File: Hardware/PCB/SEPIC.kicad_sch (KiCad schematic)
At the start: 32 parts, among them Q1 AO3401A, Q2 IRFR024PBF, U1 LM3478MA

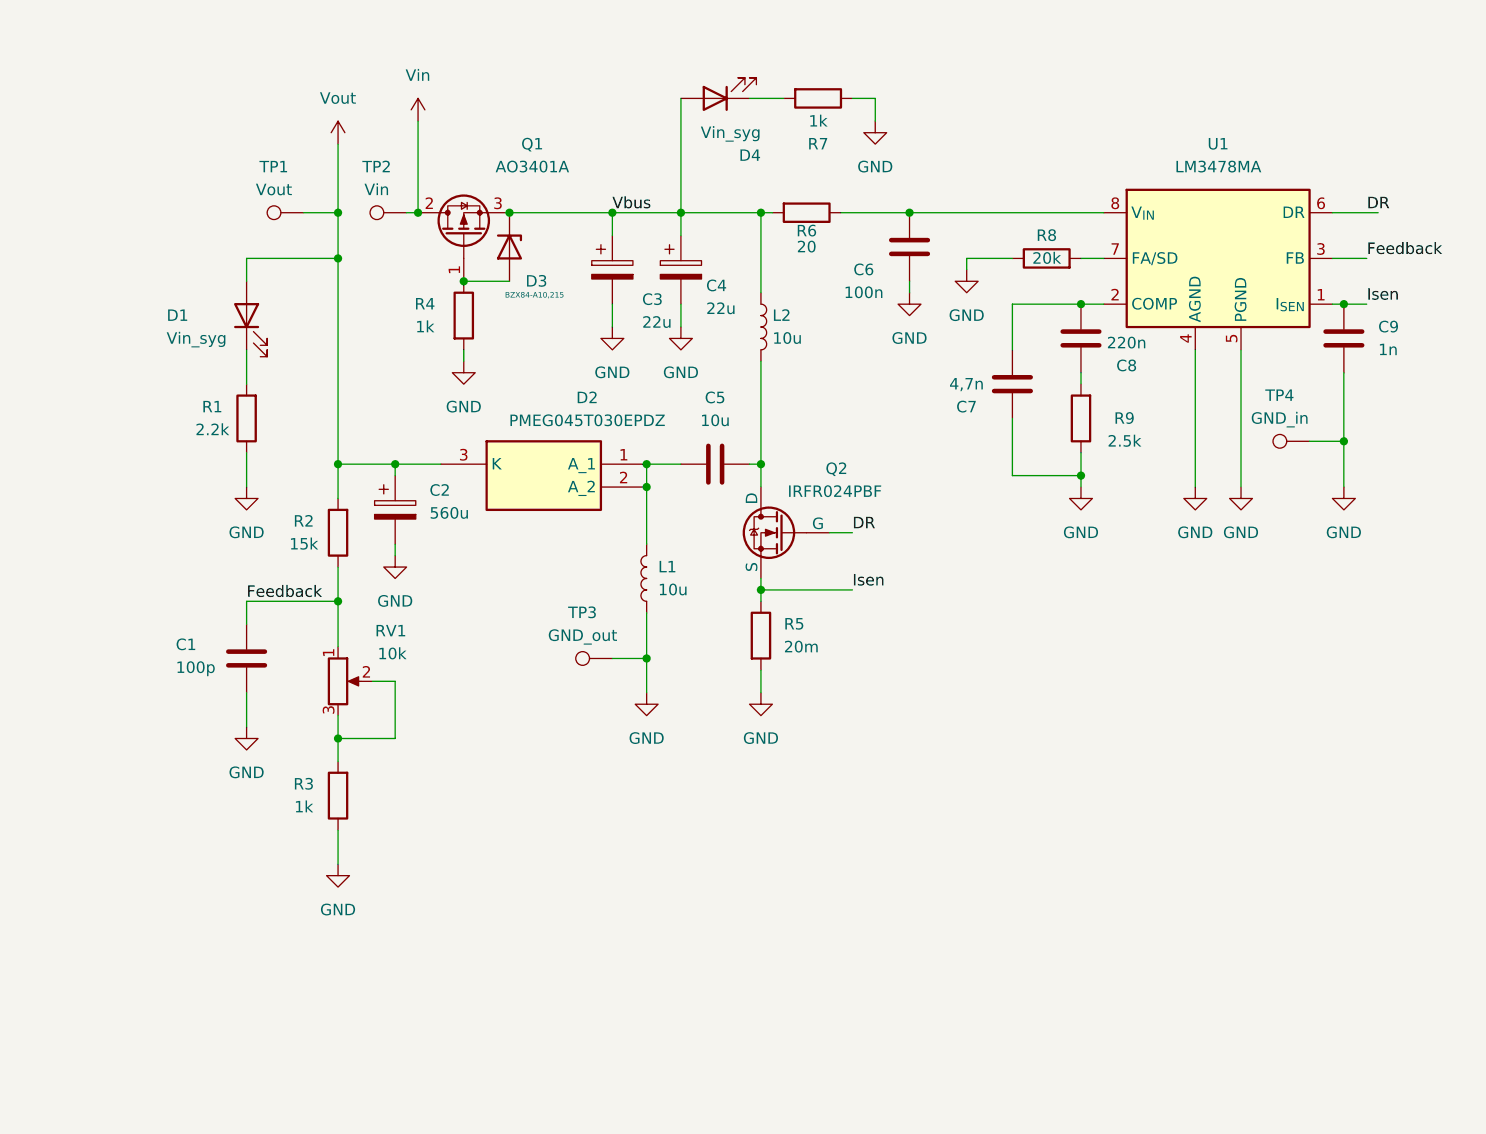
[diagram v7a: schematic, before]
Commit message: EOD PCB commit
End Of Development update, after compiling the data in a spreadsheet, I replaced the diode and the MOSFET, and also copied the calculated values for the passive components.
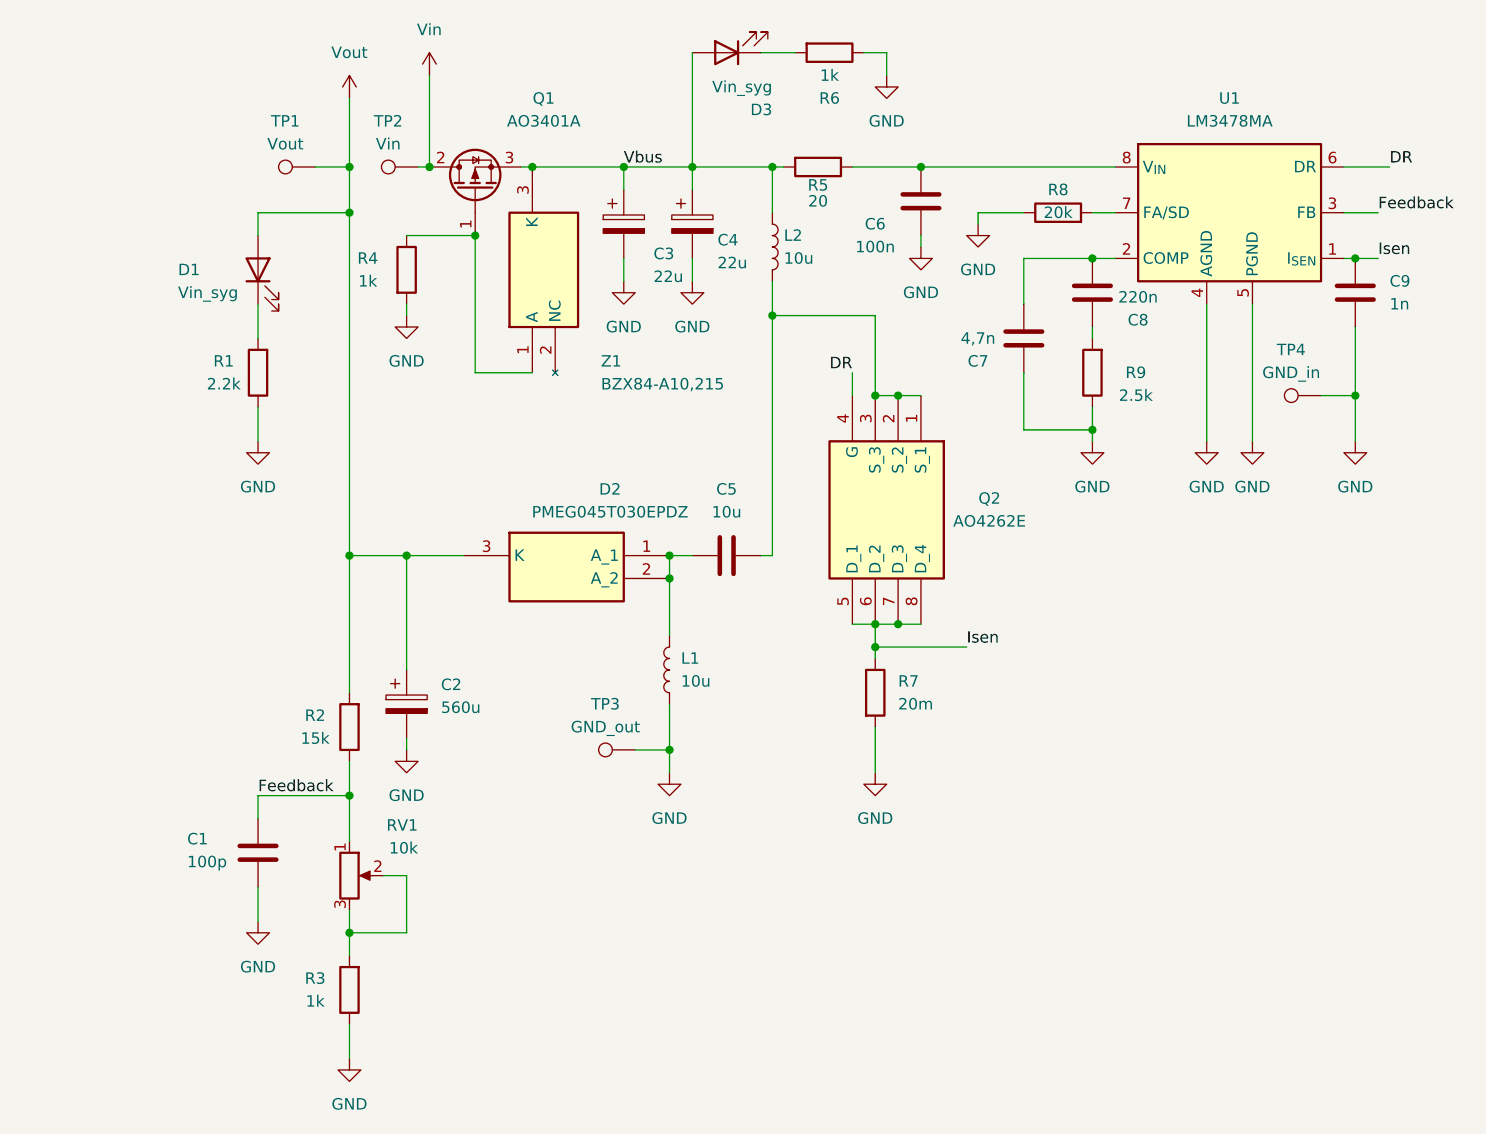
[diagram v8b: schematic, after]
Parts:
- removed D3: BZX84-A10,215, BZX84:SOT-23, symbol Device:D_Zener
- removed Q2: IRFR024PBF, IRFR024:IRFR024PBF, symbol Simulation_SPICE:NMOS
- added Q2: AO4262E, Package_SO:SOIC-8_3.9x4.9mm_P1.27mm, symbol AO4262E:AO4262E
- added Z1: BZX84-A10,215, Package_TO_SOT_SMD:SOT-23, symbol BZX84-A10_215:BZX84-A10,215
- renumbered D4 to D3, R6 to R5, R7 to R6, R5 to R7
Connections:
- net DR: now also Q2.4 (G)
- net Isen: now also Q2.5 (D_1), Q2.6 (D_2), Q2.7 (D_3), Q2.8 (D_4)
- net Vbus: now also Z1.3 (K)
- net at C5.2, L2.2: now also Q2.1 (S_1), Q2.2 (S_2), Q2.3 (S_3)
- net at Q1.1 (G), R4.1: now also Z1.1 (A)
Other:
- moved on the sheet: C1, C2, C3, C4, C5, C6, C7, C8, C9, D1, D2, D3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
